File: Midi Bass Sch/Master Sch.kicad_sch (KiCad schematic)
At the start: 31 parts, among them J1 DIN-5, J2 Master ISCP, SW2 Master Reset, U1 PIC16F1788

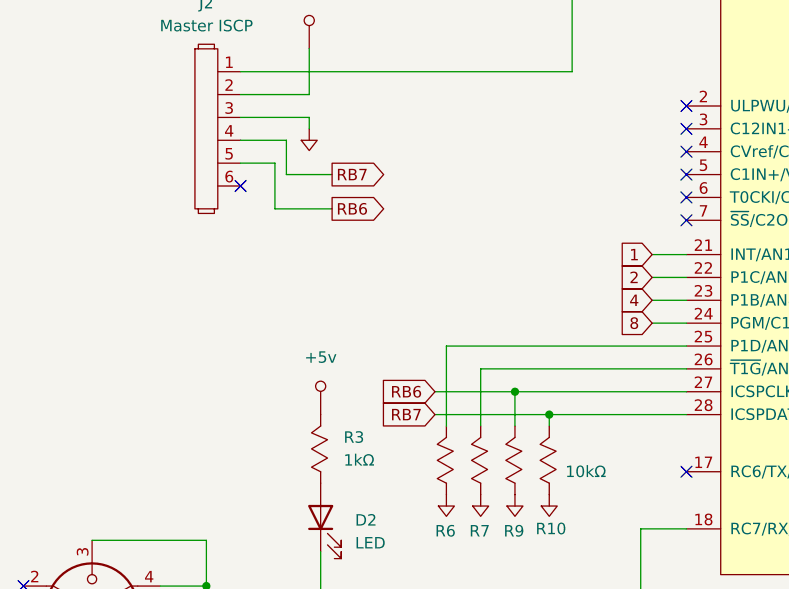
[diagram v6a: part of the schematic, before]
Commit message: added program pins to all processors
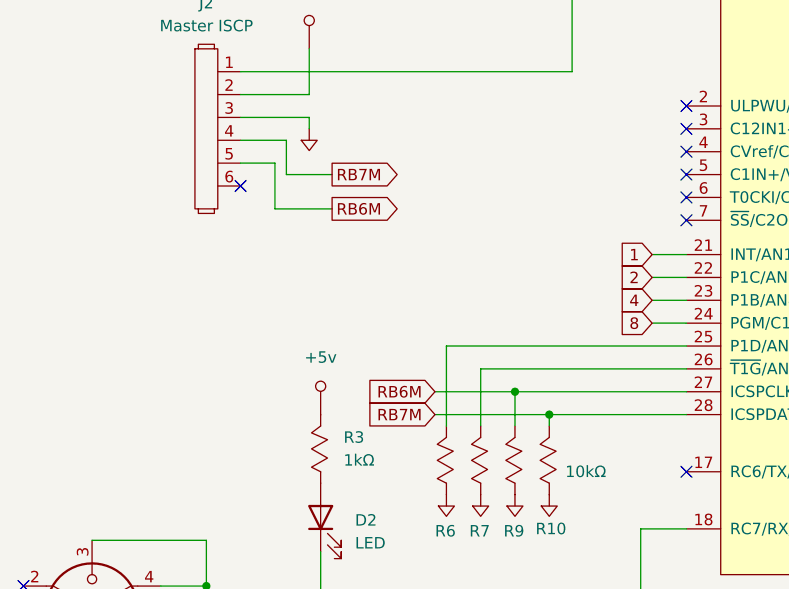
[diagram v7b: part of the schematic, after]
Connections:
- net RB6 renamed RB6M
- net RB7 renamed RB7M
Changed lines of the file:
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@@
 		)
 	)
-	(global_label "RB6"
+	(global_label "RB6M"
 		(shape output)
 		(at 58.42 67.31 0)
@@
 		)
 		(property "Intersheetrefs" "${INTERSHEET_REFS}"
-			(at 65.1547 67.31 0)
-			(effects
-				(font
-					(size 1.27 1.27)
-				)
-				(justify left)
-				(hide yes)
-			)
-		)
-	)
-	(global_label "RB7"
+			(at 66.6061 67.31 0)
+			(effects
+				(font
+					(size 1.27 1.27)
+				)
+				(justify left)
+				(hide yes)
+			)
+		)
+	)
+	(global_label "RB7M"
 		(shape input)
 		(at 69.85 90.17 180)
@@
 		)
 		(property "Intersheetrefs" "${INTERSHEET_REFS}"
-			(at 63.1153 90.17 0)
+			(at 61.6639 90.17 0)
 			(effects
 				(font
@@
 		)
 	)
-	(global_label "RB7"
+	(global_label "RB7M"
 		(shape output)
 		(at 58.42 63.5 0)
@@
 		)
 		(property "Intersheetrefs" "${INTERSHEET_REFS}"
-			(at 65.1547 63.5 0)
+			(at 66.6061 63.5 0)
 			(effects
 				(font
@@
 		)
 	)
-	(global_label "RB6"
+	(global_label "RB6M"
 		(shape input)
 		(at 69.85 87.63 180)
@@
 		)
 		(property "Intersheetrefs" "${INTERSHEET_REFS}"
-			(at 63.1153 87.63 0)
-			(effects
-				(font
+			(at 61.6639 87.63 0)
+			(effects
+				(font

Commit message: added footprints to kicad schematic still need footprint for din connector
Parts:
- C1: footprint (none) -> Capacitor_SMD:C_0805_2012Metric_Pad1.18x1.45mm_HandSolder
- D1, D2, D3, D4, D5, D6, D7: footprint (none) -> Diode_SMD:D_0805_2012Metric_Pad1.15x1.40mm_HandSolder
- J2: footprint (none) -> Connector_PinHeader_2.54mm:PinHeader_1x06_P2.54mm_Vertical
- R1, R10, R11, R12, R13, R14, R2, R3, R4, R5, R6, R7, R8, R9: footprint (none) -> Resistor_SMD:R_0805_2012Metric_Pad1.20x1.40mm_HandSolder
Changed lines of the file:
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@@
 			)
 		)
-		(property "Footprint" ""
+		(property "Footprint" "Resistor_SMD:R_0805_2012Metric_Pad1.20x1.40mm_HandSolder"
 			(at 68.58 96.52 0)
 			(effects
@@
 			)
 		)
-		(property "Footprint" ""
+		(property "Footprint" "Resistor_SMD:R_0805_2012Metric_Pad1.20x1.40mm_HandSolder"
 			(at 49.53 166.37 0)
 			(effects
@@
 			)
 		)
-		(property "Footprint" ""
+		(property "Footprint" "Resistor_SMD:R_0805_2012Metric_Pad1.20x1.40mm_HandSolder"
 			(at 72.39 96.52 0)
 			(effects
@@
 			)
 		)
-		(property "Footprint" ""
+		(property "Footprint" "Resistor_SMD:R_0805_2012Metric_Pad1.20x1.40mm_HandSolder"
 			(at 83.82 153.67 0)
 			(effects
@@
 			)
 		)
-		(property "Footprint" ""
+		(property "Footprint" "Diode_SMD:D_0805_2012Metric_Pad1.15x1.40mm_HandSolder"
 			(at 57.15 101.6 0)
 			(effects
@@
 			)
 		)
-		(property "Footprint" ""
+		(property "Footprint" "Diode_SMD:D_0805_2012Metric_Pad1.15x1.40mm_HandSolder"
 			(at 76.2 31.75 0)
 			(effects
@@
 			)
 		)
-		(property "Footprint" ""
+		(property "Footprint" "Diode_SMD:D_0805_2012Metric_Pad1.15x1.40mm_HandSolder"
 			(at 200.66 46.99 0)
 			(effects
@@
 			)
 		)
-		(property "Footprint" ""
+		(property "Footprint" "Resistor_SMD:R_0805_2012Metric_Pad1.20x1.40mm_HandSolder"
 			(at 184.15 55.88 0)
 			(effects
@@
 			)
 		)
-		(property "Footprint" ""
+		(property "Footprint" "Diode_SMD:D_0805_2012Metric_Pad1.15x1.40mm_HandSolder"
 			(at 74.93 163.83 0)
 			(effects
@@
 			)
 		)
-		(property "Footprint" ""
+		(property "Footprint" "Capacitor_SMD:C_0805_2012Metric_Pad1.18x1.45mm_HandSolder"
 			(at 67.31 30.48 0)
 			(effects
@@
 			)
 		)
-		(property "Footprint" ""
+		(property "Footprint" "Resistor_SMD:R_0805_2012Metric_Pad1.20x1.40mm_HandSolder"
 			(at 80.01 96.52 0)
 			(effects
@@
 			)
 		)
-		(property "Footprint" ""
+		(property "Footprint" "Resistor_SMD:R_0805_2012Metric_Pad1.20x1.40mm_HandSolder"
 			(at 72.39 157.48 0)
 			(effects
@@
 			)
 		)
-		(property "Footprint" ""
+		(property "Footprint" "Resistor_SMD:R_0805_2012Metric_Pad1.20x1.40mm_HandSolder"
 			(at 54.61 95.25 0)
 			(effects
@@
 			)
 		)
-		(property "Footprint" ""
+		(property "Footprint" "Resistor_SMD:R_0805_2012Metric_Pad1.20x1.40mm_HandSolder"
 			(at 44.45 38.1 0)
 			(effects
@@
 			)
 		)
-		(property "Footprint" ""
+		(property "Footprint" "Diode_SMD:D_0805_2012Metric_Pad1.15x1.40mm_HandSolder"
 			(at 52.07 172.72 0)
 			(effects
@@
 			)
 		)
-		(property "Footprint" ""
+		(property "Footprint" "Diode_SMD:D_0805_2012Metric_Pad1.15x1.40mm_HandSolder"
 			(at 86.36 160.02 0)
 			(effects
@@
 			)
 		)
-		(property "Footprint" ""
+		(property "Footprint" "Resistor_SMD:R_0805_2012Metric_Pad1.20x1.40mm_HandSolder"
 			(at 64.77 26.67 0)
 			(effects
@@
 			)
 		)
-		(property "Footprint" ""
+		(property "Footprint" "Resistor_SMD:R_0805_2012Metric_Pad1.20x1.40mm_HandSolder"
 			(at 60.96 162.56 0)
 			(effects
@@
 			)
 		)
-		(property "Footprint" ""
+		(property "Footprint" "Resistor_SMD:R_0805_2012Metric_Pad1.20x1.40mm_HandSolder"
 			(at 198.12 40.64 0)
 			(effects
@@
 			)
 		)
-		(property "Footprint" ""
+		(property "Footprint" "Diode_SMD:D_0805_2012Metric_Pad1.15x1.40mm_HandSolder"
 			(at 63.5 168.91 0)
 			(effects
@@
 			)
 		)
-		(property "Footprint" ""
+		(property "Footprint" "Resistor_SMD:R_0805_2012Metric_Pad1.20x1.40mm_HandSolder"
 			(at 76.2 96.52 0)
 			(effects
@@
 			)
 		)
-		(property "Footprint" ""
+		(property "Footprint" "Connector_PinHeader_2.54mm:PinHeader_1x06_P2.54mm_Vertical"
 			(at 44.45 48.26 0)
 			(effects
@@
 			)
 		)
-		(property "Footprint" ""
+		(property "Footprint" "Resistor_SMD:R_0805_2012Metric_Pad1.20x1.40mm_HandSolder"
 			(at 168.91 55.88 0)
 			(effects
